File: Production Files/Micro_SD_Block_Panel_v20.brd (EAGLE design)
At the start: 137.2 x 103.1 mm, 118 parts, among them U1 USD-SOCKETNEW, U10 EDISON_CONNECTOR_FULLHEADER, U11 USD-SOCKETNEW, U12 TXB0108, U13 EDISON_CONNECTOR_FULLMOUNTING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, U14 EDISON_CONNECTOR_FULLHEADER, U15 USD-SOCKETNEW, U16 TXB0108, U17 EDISON_CONNECTOR_FULLMOUNTING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, U18 EDISON_CONNECTOR_FULLHEADER, U19 USD-SOCKETNEW, U2 EDISON_CONNECTOR_FULLMOUNTING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, U20 TXB0108, U21 EDISON_CONNECTOR_FULLMOUNTING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, U22 EDISON_CONNECTOR_FULLHEADER, U23 USD-SOCKETNEW, U24 TXB0108, U25 EDISON_CONNECTOR_FULLMOUNTING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, U26 EDISON_CONNECTOR_FULLHEADER, U27 USD-SOCKETNEW, U28 TXB0108, U29 EDISON_CONNECTOR_FULLMOUNTING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, U3 EDISON_CONNECTOR_FULLHEADER, U30 EDISON_CONNECTOR_FULLHEADER, U31 USD-SOCKETNEW, U32 TXB0108, U4 TXB0108, U5 EDISON_CONNECTOR_FULLMOUNTING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, U6 EDISON_CONNECTOR_FULLHEADER, U7 USD-SOCKETNEW, U8 TXB0108, U9 EDISON_CONNECTOR_FULLMOUNTING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

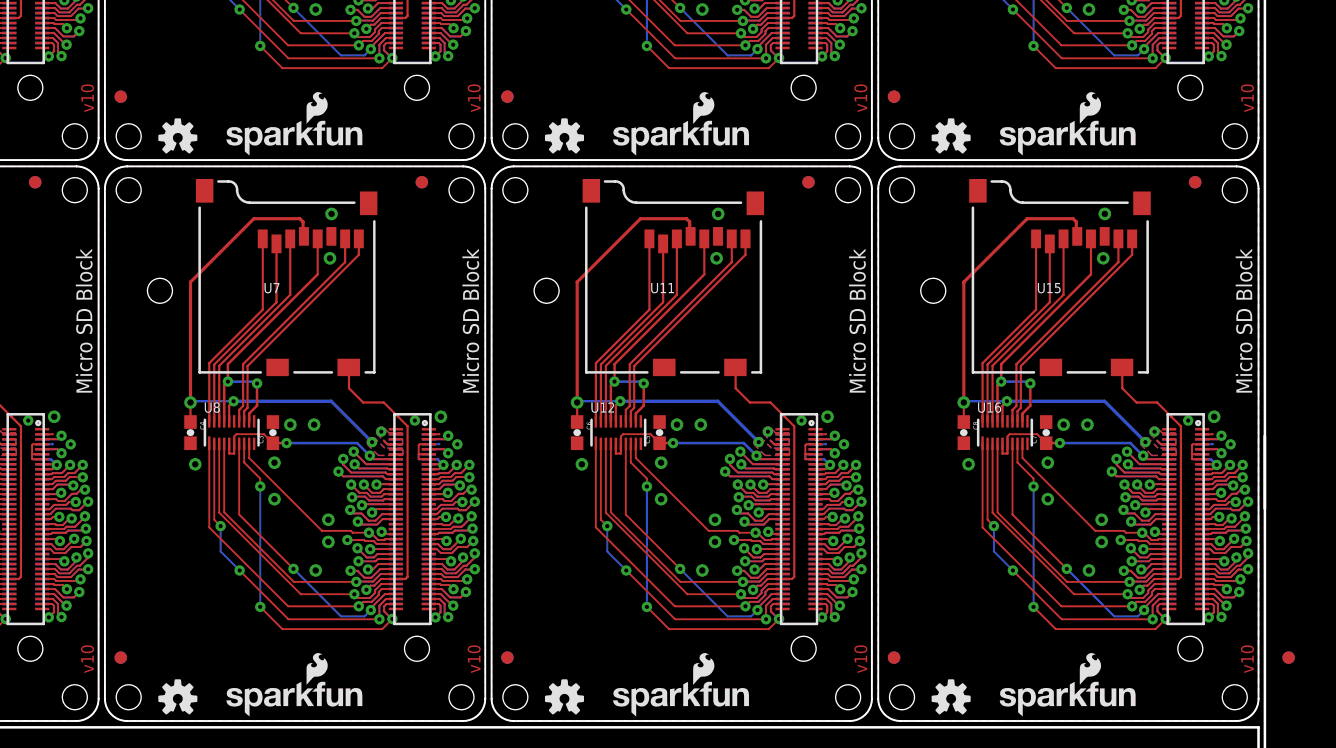
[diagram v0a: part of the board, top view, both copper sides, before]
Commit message: removed v10 panels and created v20 panels
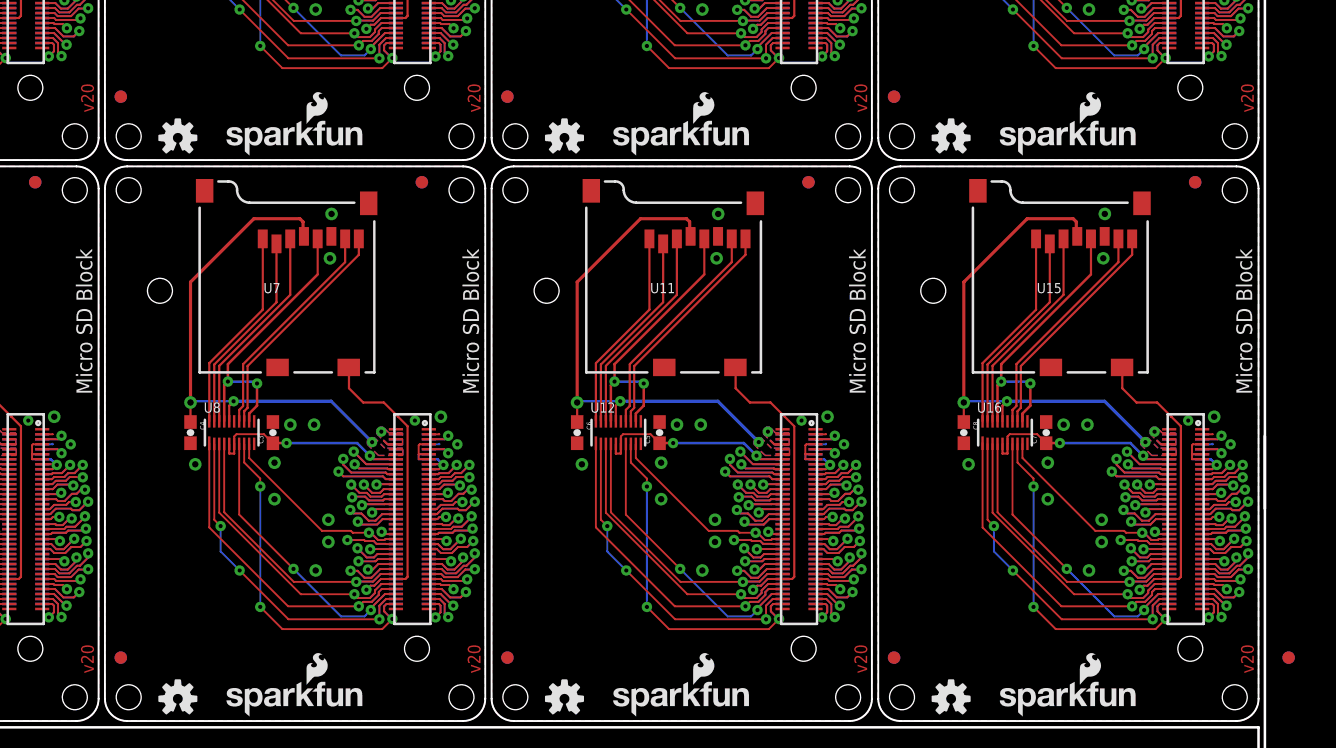
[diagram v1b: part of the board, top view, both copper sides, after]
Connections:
- net GND: no longer U1.CD2
- net GND1: no longer U7.CD2
- net GND2: no longer U11.CD2
- net GND3: no longer U15.CD2
- net GND4: no longer U19.CD2
- net GND5: no longer U23.CD2
- net GND6: no longer U27.CD2
- net GND7: no longer U31.CD2
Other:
- board text added: "v20"
- board text removed: "v10"
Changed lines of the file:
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@@
 <?xml version="1.0" encoding="utf-8"?>
 <!DOCTYPE eagle SYSTEM "eagle.dtd">
-<eagle version="6.6.0">
+<eagle version="7.2.0">
 <drawing>
 <settings>
@@
 <rectangle x1="28.956" y1="33.02" x2="37.338" y2="51.308" layer="41" rot="R180"/>
 <text x="36.068" y="13.208" size="1.016" layer="22" font="vector" ratio="15" rot="SMR270" align="center">4xM2.0</text>
-<text x="36.957" y="10.668" size="1.016" layer="1" font="vector" ratio="15" rot="R90">v10</text>
+<text x="36.957" y="10.668" size="1.016" layer="1" font="vector" ratio="15" rot="R90">v20</text>
 <text x="36.83" y="48.006" size="1.27" layer="22" font="vector" ratio="15" rot="SMR270">Micro SD Block</text>
 <wire x1="29.6672" y1="30.0482" x2="30.6578" y2="30.0482" width="0.1524" layer="42"/>
@@
 <rectangle x1="59.944" y1="33.02" x2="68.326" y2="51.308" layer="41" rot="R180"/>
 <text x="67.056" y="13.208" size="1.016" layer="22" font="vector" ratio="15" rot="SMR270" align="center">4xM2.0</text>
-<text x="67.945" y="10.668" size="1.016" layer="1" font="vector" ratio="15" rot="R90">v10</text>
+<text x="67.945" y="10.668" size="1.016" layer="1" font="vector" ratio="15" rot="R90">v20</text>
 <text x="67.818" y="48.006" size="1.27" layer="22" font="vector" ratio="15" rot="SMR270">Micro SD Block</text>
 <wire x1="60.6552" y1="30.0482" x2="61.6458" y2="30.0482" width="0.1524" layer="42"/>
@@
 <rectangle x1="90.932" y1="33.02" x2="99.314" y2="51.308" layer="41" rot="R180"/>
 <text x="98.044" y="13.208" size="1.016" layer="22" font="vector" ratio="15" rot="SMR270" align="center">4xM2.0</text>
-<text x="98.933" y="10.668" size="1.016" layer="1" font="vector" ratio="15" rot="R90">v10</text>
+<text x="98.933" y="10.668" size="1.016" layer="1" font="vector" ratio="15" rot="R90">v20</text>
 <text x="98.806" y="48.006" size="1.27" layer="22" font="vector" ratio="15" rot="SMR270">Micro SD Block</text>
 <wire x1="91.6432" y1="30.0482" x2="92.6338" y2="30.0482" width="0.1524" layer="42"/>
@@
 <rectangle x1="121.92" y1="33.02" x2="130.302" y2="51.308" layer="41" rot="R180"/>
 <text x="129.032" y="13.208" size="1.016" layer="22" font="vector" ratio="15" rot="SMR270" align="center">4xM2.0</text>
-<text x="129.921" y="10.668" size="1.016" layer="1" font="vector" ratio="15" rot="R90">v10</text>
+<text x="129.921" y="10.668" size="1.016" layer="1" font="vector" ratio="15" rot="R90">v20</text>
 <text x="129.794" y="48.006" size="1.27" layer="22" font="vector" ratio="15" rot="SMR270">Micro SD Block</text>
 <wire x1="122.6312" y1="30.0482" x2="123.6218" y2="30.0482" width="0.1524" layer="42"/>
@@
 <rectangle x1="28.956" y1="77.978" x2="37.338" y2="96.266" layer="41" rot="R180"/>
 <text x="36.068" y="58.166" size="1.016" layer="22" font="vector" ratio="15" rot="SMR270" align="center">4xM2.0</text>
-<text x="36.957" y="55.626" size="1.016" layer="1" font="vector" ratio="15" rot="R90">v10</text>
+<text x="36.957" y="55.626" size="1.016" layer="1" font="vector" ratio="15" rot="R90">v20</text>
 <text x="36.83" y="92.964" size="1.27" layer="22" font="vector" ratio="15" rot="SMR270">Micro SD Block</text>
 <wire x1="29.6672" y1="75.0062" x2="30.6578" y2="75.0062" width="0.1524" layer="42"/>
@@
 <rectangle x1="59.944" y1="77.978" x2="68.326" y2="96.266" layer="41" rot="R180"/>
 <text x="67.056" y="58.166" size="1.016" layer="22" font="vector" ratio="15" rot="SMR270" align="center">4xM2.0</text>
-<text x="67.945" y="55.626" size="1.016" layer="1" font="vector" ratio="15" rot="R90">v10</text>
+<text x="67.945" y="55.626" size="1.016" layer="1" font="vector" ratio="15" rot="R90">v20</text>
 <text x="67.818" y="92.964" size="1.27" layer="22" font="vector" ratio="15" rot="SMR270">Micro SD Block</text>
 <wire x1="60.6552" y1="75.0062" x2="61.6458" y2="75.0062" width="0.1524" layer="42"/>
@@
 <rectangle x1="90.932" y1="77.978" x2="99.314" y2="96.266" layer="41" rot="R180"/>
 <text x="98.044" y="58.166" size="1.016" layer="22" font="vector" ratio="15" rot="SMR270" align="center">4xM2.0</text>
-<text x="98.933" y="55.626" size="1.016" layer="1" font="vector" ratio="15" rot="R90">v10</text>
+<text x="98.933" y="55.626" size="1.016" layer="1" font="vector" ratio="15" rot="R90">v20</text>
 <text x="98.806" y="92.964" size="1.27" layer="22" font="vector" ratio="15" rot="SMR270">Micro SD Block</text>
 <wire x1="91.6432" y1="75.0062" x2="92.6338" y2="75.0062" width="0.1524" layer="42"/>
@@
 <rectangle x1="121.92" y1="77.978" x2="130.302" y2="96.266" layer="41" rot="R180"/>
 <text x="129.032" y="58.166" size="1.016" layer="22" font="vector" ratio="15" rot="SMR270" align="center">4xM2.0</text>
-<text x="129.921" y="55.626" size="1.016" layer="1" font="vector" ratio="15" rot="R90">v10</text>
+<text x="129.921" y="55.626" size="1.016" layer="1" font="vector" ratio="15" rot="R90">v20</text>
 <text x="129.794" y="92.964" size="1.27" layer="22" font="vector" ratio="15" rot="SMR270">Micro SD Block</text>
 <wire x1="122.6312" y1="75.0062" x2="123.6218" y2="75.0062" width="0.1524" layer="42"/>
@@
 <pass name="Default">
 <param name="RoutingGrid" value="50mil"/>
+<param name="AutoGrid" value="1"/>
+<param name="Efforts" value="0"/>
+<param name="TopRouterVariant" value="1"/>
 <param name="tpViaShape" value="round"/>
 <param name="PrefDir.1" value="|"/>
@@
 <contactref element="U3" pad="13"/>
 <contactref element="U1" pad="GND3"/>
-<contactref element="U1" pad="CD2"/>
 <contactref element="U1" pad="GND1"/>
 <contactref element="U4" pad="P$15"/>
@@
 <contactref element="U6" pad="13"/>
 <contactref element="U7" pad="GND3"/>
-<contactref element="U7" pad="CD2"/>
 <contactref element="U7" pad="GND1"/>
 <contactref element="U8" pad="P$15"/>
@@
 <contactref element="U10" pad="13"/>
 <contactref element="U11" pad="GND3"/>
-<contactref element="U11" pad="CD2"/>
 <contactref element="U11" pad="GND1"/>
 <contactref element="U12" pad="P$15"/>
@@
 <contactref element="U14" pad="13"/>
 <contactref element="U15" pad="GND3"/>
-<contactref element="U15" pad="CD2"/>
 <contactref element="U15" pad="GND1"/>
 <contactref element="U16" pad="P$15"/>
@@
 <contactref element="U18" pad="13"/>
 <contactref element="U19" pad="GND3"/>
-<contactref element="U19" pad="CD2"/>
 <contactref element="U19" pad="GND1"/>
 <contactref element="U20" pad="P$15"/>
@@
 <contactref element="U22" pad="13"/>
 <contactref element="U23" pad="GND3"/>
-<contactref element="U23" pad="CD2"/>
 <contactref element="U23" pad="GND1"/>
 <contactref element="U24" pad="P$15"/>
@@
 <contactref element="U26" pad="13"/>
 <contactref element="U27" pad="GND3"/>
-<contactref element="U27" pad="CD2"/>
 <contactref element="U27" pad="GND1"/>
 <contactref element="U28" pad="P$15"/>
@@
 <contactref element="U30" pad="13"/>
 <contactref element="U31" pad="GND3"/>
-<contactref element="U31" pad="CD2"/>
 <contactref element="U31" pad="GND1"/>
 <contactref element="U32" pad="P$15"/>
